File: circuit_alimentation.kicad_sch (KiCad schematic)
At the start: 32 parts, among them U1 STM32-(STM32H745ZIT6)

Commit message: Plein de modifs
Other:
- note added: "À vérifier si peux convertir 5V en 3.3V (voir VDD50USB)"
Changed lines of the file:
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@@
+    (stroke (width 0) (type default))
+  )
+  (wire (pts (xy 25.4 88.9) (xy 31.75 88.9))
     (stroke (width 0) (type default))
   )
@@
     (fill (type none))
   )
+  (arc (start 12.7 99.06) (mid 12.7638 93.8259) (end 16.51 90.17)
+    (stroke (width 0) (type default))
+    (fill (type none))
+  )
   (text "Découplage" (at 215.9 16.51 0)
+    (effects (font (size 1.27 1.27)) (justify left bottom))
+  )
+  (text "À vérifier si peux convertir\n5V en 3.3V (voir VDD50USB)"
+    (at 13.97 102.87 0)
     (effects (font (size 1.27 1.27)) (justify left bottom))
   )
@@
     )
   )
+  (symbol (lib_id "power:GND") (at 25.4 88.9 270) (unit 1)
+    (in_bom yes) (on_board yes) (dnp no) (fields_autoplaced)
+    (property "Reference" "#PWR059" (at 19.05 88.9 0)
+      (effects (font (size 1.27 1.27)) hide)
+    )
+    (property "Value" "GND" (at 21.59 88.9 90)
+      (effects (font (size 1.27 1.27)) (justify right))
+    )
+    (property "Footprint" "" (at 25.4 88.9 0)
+      (effects (font (size 1.27 1.27)) hide)
+    )
+    (property "Datasheet" "" (at 25.4 88.9 0)
+      (effects (font (size 1.27 1.27)) hide)
+    )
+    (pin "1")
+    (instances
+      (project "Payload"
+        (path "/5f62c44b-34ee-4720-b187-b4a520863a8a/b20c1a40-233f-480d-ac91-6f1a7bcdc93c"
+          (reference "#PWR059") (unit 1)
+        )
+      )
+    )
+  )
   (symbol (lib_id "power:+3.3V") (at 250.19 109.22 0) (unit 1)
     (in_bom yes) (on_board yes) (dnp no) (fields_autoplaced)
@@
         )
       )
-    )
-  )
-  (symbol (lib_id "power:GND") (at 31.75 88.9 270) (unit 1)
-    (in_bom yes) (on_board yes) (dnp no) (fields_autoplaced)
-    (property "Reference" "#PWR059" (at 25.4 88.9 0)
-      (effects (font (size 1.27 1.27)) hide)
-    )
-    (property "Value" "GND" (at 27.94 88.9 90)
-      (effects (font (size 1.27 1.27)) (justify right))
-    )
-    (property "Footprint" "" (at 31.75 88.9 0)
-      (effects (font (size 1.27 1.27)) hide)
-    )
-    (property "Datasheet" "" (at 31.75 88.9 0)
-      (effects (font (size 1.27 1.27)) hide)
-    )
-    (pin "1")
-    (instances
-      (project "Payload"
-        (path "/5f62c44b-34ee-4720-b187-b4a520863a8a/b20c1a40-233f-480d-ac91-6f1a7bcdc93c"
-          (reference "#PWR059") (unit 1)
-        )
-      )

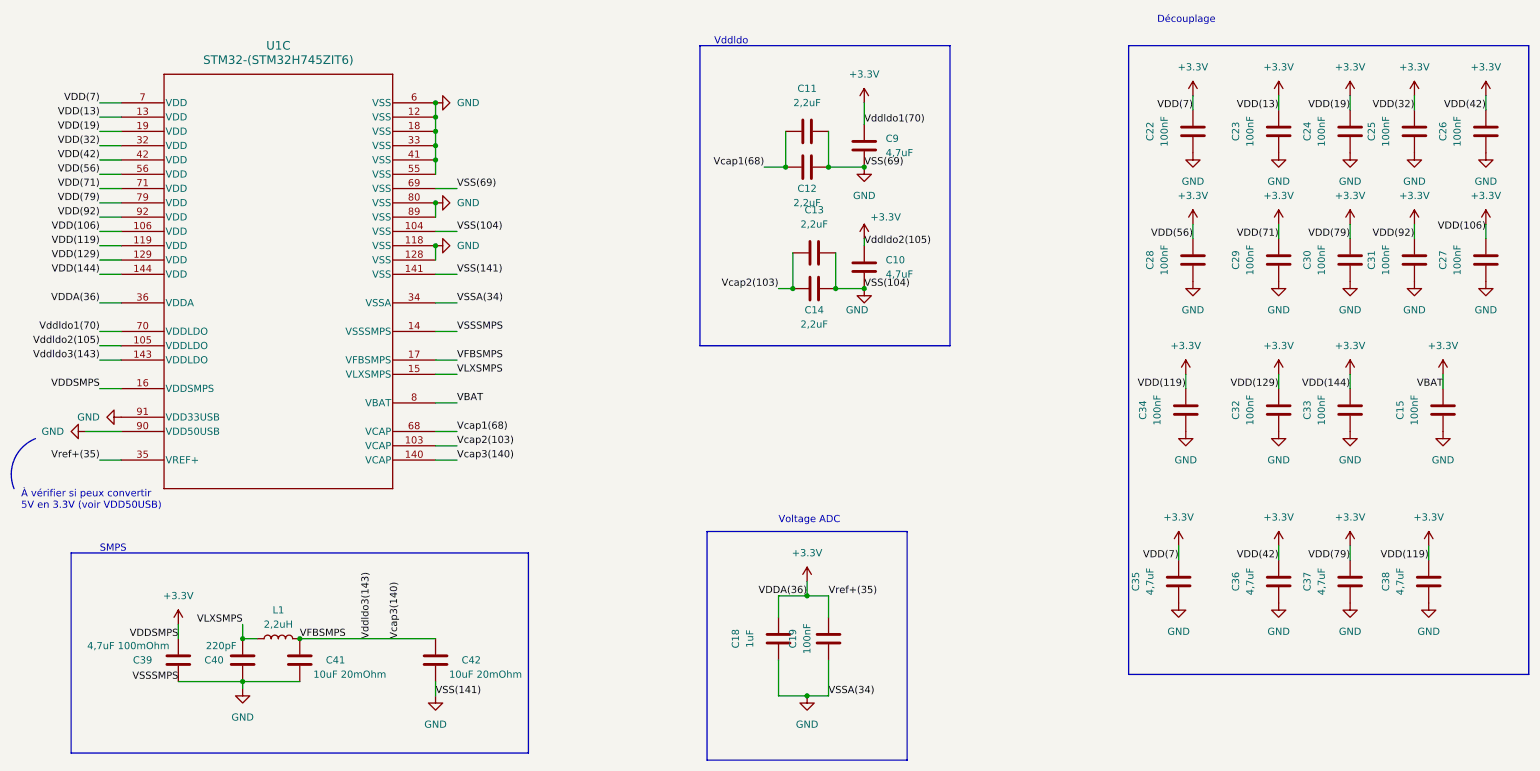
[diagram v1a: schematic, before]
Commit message: Petites modif et assignation des empreintes à 50%
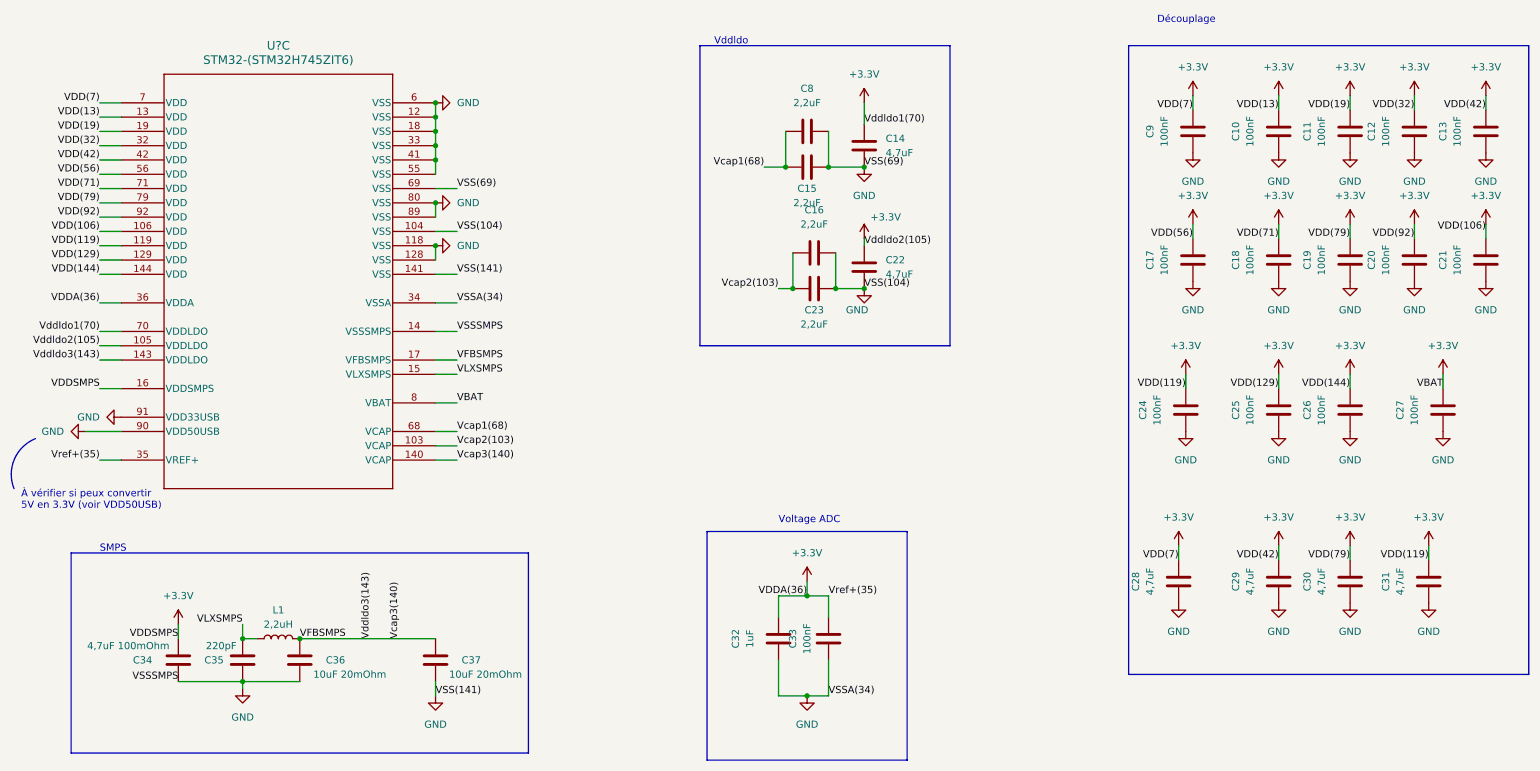
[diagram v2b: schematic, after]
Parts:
- C10: renamed from C23; footprint (none) -> GAUL-Empreintes:cap-0.1uF-(CAPC0603X33N)
- C11: renamed from C24; footprint (none) -> GAUL-Empreintes:cap-0.1uF-(CAPC0603X33N)
- C12: renamed from C25; footprint (none) -> GAUL-Empreintes:cap-0.1uF-(CAPC0603X33N)
- C13: renamed from C26; footprint (none) -> GAUL-Empreintes:cap-0.1uF-(CAPC0603X33N)
- C15: renamed from C12; footprint (none) -> GAUL-Empreintes:cap-2.2uF-(CAPC1005X55N)
- C16: renamed from C13; footprint (none) -> GAUL-Empreintes:cap-2.2uF-(CAPC1005X55N)
- C17: renamed from C28; footprint (none) -> GAUL-Empreintes:cap-0.1uF-(CAPC0603X33N)
- C18: renamed from C29; footprint (none) -> GAUL-Empreintes:cap-0.1uF-(CAPC0603X33N)
- C19: renamed from C30; footprint (none) -> GAUL-Empreintes:cap-0.1uF-(CAPC0603X33N)
- C20: renamed from C31; footprint (none) -> GAUL-Empreintes:cap-0.1uF-(CAPC0603X33N)
- C21: renamed from C27; footprint (none) -> GAUL-Empreintes:cap-0.1uF-(CAPC0603X33N)
- C23: renamed from C14; footprint (none) -> GAUL-Empreintes:cap-2.2uF-(CAPC1005X55N)
- C24: renamed from C34; footprint (none) -> GAUL-Empreintes:cap-0.1uF-(CAPC0603X33N)
- C25: renamed from C32; footprint (none) -> GAUL-Empreintes:cap-0.1uF-(CAPC0603X33N)
- C26: renamed from C33; footprint (none) -> GAUL-Empreintes:cap-0.1uF-(CAPC0603X33N)
- C27: renamed from C15; footprint (none) -> GAUL-Empreintes:cap-0.1uF-(CAPC0603X33N)
- C28: renamed from C35; footprint (none) -> GAUL-Empreintes:cap-4.7uF-(CAPC1608X90N)
- C29: renamed from C36; footprint (none) -> GAUL-Empreintes:cap-4.7uF-(CAPC1608X90N)
- C30: renamed from C37; footprint (none) -> GAUL-Empreintes:cap-4.7uF-(CAPC1608X90N)
- C31: renamed from C38; footprint (none) -> GAUL-Empreintes:cap-4.7uF-(CAPC1608X90N)
- C32: renamed from C18; footprint (none) -> GAUL-Empreintes:cap-1uF-(CAPC0603X35N)
- C33: renamed from C19; footprint (none) -> GAUL-Empreintes:cap-0.1uF-(CAPC0603X33N)
- C9: renamed from C22; footprint (none) -> GAUL-Empreintes:cap-0.1uF-(CAPC0603X33N)
- U?: renamed from U1; footprint LQFP-144 -> GAUL-Empreintes:STM32
- renumbered C9 to C14, C10 to C22, C39 to C34, C40 to C35, C41 to C36, C42 to C37, C11 to C8

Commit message: Début PCB
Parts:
- C10, C11, C12, C13, C17, C18, C19, C20, C21, C24, C25, C26, C27, C33, C9: footprint GAUL-Empreintes:cap-0.1uF-(CAPC0603X33N) -> Capacitor_SMD:C_0603_1608Metric_Pad1.08x0.95mm_HandSolder
- C14, C22, C35, C8: footprint (none) -> Capacitor_SMD:C_0603_1608Metric_Pad1.08x0.95mm_HandSolder
- C15, C16, C23: footprint GAUL-Empreintes:cap-2.2uF-(CAPC1005X55N) -> Capacitor_SMD:C_0603_1608Metric_Pad1.08x0.95mm_HandSolder
- C28, C29, C30, C31: footprint GAUL-Empreintes:cap-4.7uF-(CAPC1608X90N) -> Capacitor_SMD:C_0603_1608Metric_Pad1.08x0.95mm_HandSolder
- C32: footprint GAUL-Empreintes:cap-1uF-(CAPC0603X35N) -> Capacitor_SMD:C_0603_1608Metric_Pad1.08x0.95mm_HandSolder
- C34: footprint (none) -> GAUL-Empreintes:cap-4.7uF-75R-(CAPMP7.6X4.3_3.1N_KEM-L)
- C36, C37: footprint (none) -> GAUL-Empreintes:cap-10uF-50R-(CAPMP7.6X4.3_4.3N_KEM-L)
- L1: footprint (none) -> Inductor_SMD:L_0603_1608Metric_Pad1.05x0.95mm_HandSolder
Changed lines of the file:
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@@
       (effects (font (size 1.27 1.27)))
     )
-    (property "Footprint" "GAUL-Empreintes:cap-0.1uF-(CAPC0603X33N)" (at 273.3548 54.61 0)
+    (property "Footprint" "Capacitor_SMD:C_0603_1608Metric_Pad1.08x0.95mm_HandSolder" (at 273.3548 54.61 0)
       (effects (font (size 1.27 1.27)) hide)
     )
@@
       (effects (font (size 1.27 1.27)))
     )
-    (property "Footprint" "GAUL-Empreintes:cap-0.1uF-(CAPC0603X33N)" (at 260.6548 54.61 0)
+    (property "Footprint" "Capacitor_SMD:C_0603_1608Metric_Pad1.08x0.95mm_HandSolder" (at 260.6548 54.61 0)
       (effects (font (size 1.27 1.27)) hide)
     )
@@
       (effects (font (size 1.27 1.27)))
     )
-    (property "Footprint" "GAUL-Empreintes:cap-0.1uF-(CAPC0603X33N)" (at 236.5248 54.61 0)
+    (property "Footprint" "Capacitor_SMD:C_0603_1608Metric_Pad1.08x0.95mm_HandSolder" (at 236.5248 54.61 0)
       (effects (font (size 1.27 1.27)) hide)
     )
@@
       (effects (font (size 1.27 1.27)))
     )
-    (property "Footprint" "GAUL-Empreintes:cap-2.2uF-(CAPC1005X55N)" (at 158.75 62.5348 0)
+    (property "Footprint" "Capacitor_SMD:C_0603_1608Metric_Pad1.08x0.95mm_HandSolder" (at 158.75 62.5348 0)
       (effects (font (size 1.27 1.27)) hide)
     )
@@
       (effects (font (size 1.27 1.27)))
     )
-    (property "Footprint" "GAUL-Empreintes:cap-4.7uF-(CAPC1608X90N)" (at 218.7448 111.76 0)
+    (property "Footprint" "Capacitor_SMD:C_0603_1608Metric_Pad1.08x0.95mm_HandSolder" (at 218.7448 111.76 0)
       (effects (font (size 1.27 1.27)) hide)
     )
@@
       (effects (font (size 1.27 1.27)))
     )
-    (property "Footprint" "GAUL-Empreintes:cap-2.2uF-(CAPC1005X55N)" (at 158.75 56.1848 0)
+    (property "Footprint" "Capacitor_SMD:C_0603_1608Metric_Pad1.08x0.95mm_HandSolder" (at 158.75 56.1848 0)
       (effects (font (size 1.27 1.27)) hide)
     )
@@
       (effects (font (size 1.27 1.27)))
     )
-    (property "Footprint" "GAUL-Empreintes:cap-1uF-(CAPC0603X35N)" (at 147.6248 121.92 0)
+    (property "Footprint" "Capacitor_SMD:C_0603_1608Metric_Pad1.08x0.95mm_HandSolder" (at 147.6248 121.92 0)
       (effects (font (size 1.27 1.27)) hide)
     )
@@
       (effects (font (size 1.27 1.27)))
     )
-    (property "Footprint" "GAUL-Empreintes:cap-0.1uF-(CAPC0603X33N)" (at 221.2848 31.75 0)
+    (property "Footprint" "Capacitor_SMD:C_0603_1608Metric_Pad1.08x0.95mm_HandSolder" (at 221.2848 31.75 0)
       (effects (font (size 1.27 1.27)) hide)
     )
@@
       (effects (font (size 1.27 1.27)) (justify right))
     )
-    (property "Footprint" "" (at 162.8648 55.88 0)
+    (property "Footprint" "Capacitor_SMD:C_0603_1608Metric_Pad1.08x0.95mm_HandSolder" (at 162.8648 55.88 0)
       (effects (font (size 1.27 1.27)) hide)
     )
@@
       (effects (font (size 1.27 1.27)))
     )
-    (property "Footprint" "GAUL-Empreintes:cap-4.7uF-(CAPC1608X90N)" (at 263.1948 111.76 0)
+    (property "Footprint" "Capacitor_SMD:C_0603_1608Metric_Pad1.08x0.95mm_HandSolder" (at 263.1948 111.76 0)
       (effects (font (size 1.27 1.27)) hide)
     )
@@
       (effects (font (size 1.27 1.27)))
     )
-    (property "Footprint" "" (at 86.6648 125.73 0)
+    (property "Footprint" "GAUL-Empreintes:cap-10uF-50R-(CAPMP7.6X4.3_4.3N_KEM-L)" (at 86.6648 125.73 0)
       (effects (font (size 1.27 1.27)) hide)
     )
@@
       (effects (font (size 1.27 1.27)))
     )
-    (property "Footprint" "GAUL-Empreintes:cap-4.7uF-(CAPC1608X90N)" (at 249.2248 111.76 0)
+    (property "Footprint" "Capacitor_SMD:C_0603_1608Metric_Pad1.08x0.95mm_HandSolder" (at 249.2248 111.76 0)
       (effects (font (size 1.27 1.27)) hide)
     )
@@
       (effects (font (size 1.27 1.27)))
     )
-    (property "Footprint" "" (at 59.69 125.73 0)
+    (property "Footprint" "Inductor_SMD:L_0603_1608Metric_Pad1.05x0.95mm_HandSolder" (at 59.69 125.73 0)
       (effects (font (size 1.27 1.27)) hide)
     )
@@
       (effects (font (size 1.27 1.27)))
     )
-    (property "Footprint" "GAUL-Empreintes:cap-0.1uF-(CAPC0603X33N)" (at 236.5248 81.28 0)
+    (property "Footprint" "Capacitor_SMD:C_0603_1608Metric_Pad1.08x0.95mm_HandSolder" (at 236.5248 81.28 0)
       (effects (font (size 1.27 1.27)) hide)
     )
@@
       (effects (font (size 1.27 1.27)))
     )
-    (property "Footprint" "GAUL-Empreintes:cap-0.1uF-(CAPC0603X33N)" (at 249.2248 31.75 0)
+    (property "Footprint" "Capacitor_SMD:C_0603_1608Metric_Pad1.08x0.95mm_HandSolder" (at 249.2248 31.75 0)
       (effects (font (size 1.27 1.27)) hide)
     )
@@
       (effects (font (size 1.27 1.27)))
     )
-    (property "Footprint" "GAUL-Empreintes:cap-0.1uF-(CAPC0603X33N)" (at 260.6548 31.75 0)
+    (property "Footprint" "Capacitor_SMD:C_0603_1608Metric_Pad1.08x0.95mm_HandSolder" (at 260.6548 31.75 0)
       (effects (font (size 1.27 1.27)) hide)
     )
@@
       (effects (font (size 1.27 1.27)))
     )
-    (property "Footprint" "GAUL-Empreintes:cap-0.1uF-(CAPC0603X33N)" (at 221.2848 54.61 0)
+    (property "Footprint" "Capacitor_SMD:C_0603_1608Metric_Pad1.08x0.95mm_HandSolder" (at 221.2848 54.61 0)
       (effects (font (size 1.27 1.27)) hide)
     )
@@
       (effects (font (size 1.27 1.27)))
     )
-    (property "Footprint" "GAUL-Empreintes:cap-0.1uF-(CAPC0603X33N)" (at 249.2248 81.28 0)
+    (property "Footprint" "Capacitor_SMD:C_0603_1608Metric_Pad1.08x0.95mm_HandSolder" (at 249.2248 81.28 0)
       (effects (font (size 1.27 1.27)) hide)
     )
@@
       (effects (font (size 1.27 1.27)))
     )
-    (property "Footprint" "" (at 42.8752 133.35 0)
+    (property "Footprint" "GAUL-Empreintes:cap-4.7uF-75R-(CAPMP7.6X4.3_3.1N_KEM-L)" (at 42.8752 133.35 0)
       (effects (font (size 1.27 1.27)) hide)
     )
@@
       (effects (font (size 1.27 1.27)))
     )
-    (property "Footprint" "GAUL-Empreintes:cap-4.7uF-(CAPC1608X90N)" (at 236.5248 111.76 0)
+    (property "Footprint" "Capacitor_SMD:C_0603_1608Metric_Pad1.08x0.95mm_HandSolder" (at 236.5248 111.76 0)
       (effects (font (size 1.27 1.27)) hide)
     )
@@
       (effects (font (size 1.27 1.27)))
     )
-    (property "Footprint" "GAUL-Empreintes:cap-0.1uF-(CAPC0603X33N)" (at 236.5248 31.75 0)
+    (property "Footprint" "Capacitor_SMD:C_0603_1608Metric_Pad1.08x0.95mm_HandSolder" (at 236.5248 31.75 0)
       (effects (font (size 1.27 1.27)) hide)
     )
@@
       (effects (font (size 1.27 1.27)))
     )
-    (property "Footprint" "GAUL-Empreintes:cap-2.2uF-(CAPC1005X55N)" (at 157.48 40.9448 0)
+    (property "Footprint" "Capacitor_SMD:C_0603_1608Metric_Pad1.08x0.95mm_HandSolder" (at 157.48 40.9448 0)
       (effects (font (size 1.27 1.27)) hide)
     )
@@
       (effects (font (size 1.27 1.27)))
     )
-    (property "Footprint" "" (at 54.3052 133.35 0)
+    (property "Footprint" "Capacitor_SMD:C_0603_1608Metric_Pad1.08x0.95mm_HandSolder" (at 54.3052 133.35 0)
       (effects (font (size 1.27 1.27)) hide)
     )
@@
       (effects (font (size 1.27 1.27)))
     )
-    (property "Footprint" "" (at 157.48 34.5948 0)
+    (property "Footprint" "Capacitor_SMD:C_0603_1608Metric_Pad1.08x0.95mm_HandSolder" (at 157.48 34.5948 0)
       (effects (font (size 1.27 1.27)) hide)
     )
@@
       (effects (font (size 1.27 1.27)))
     )
-    (property "Footprint" "GAUL-Empreintes:cap-0.1uF-(CAPC0603X33N)" (at 249.2248 54.61 0)
+    (property "Footprint" "Capacitor_SMD:C_0603_1608Metric_Pad1.08x0.95mm_HandSolder" (at 249.2248 54.61 0)
       (effects (font (size 1.27 1.27)) hide)
     )
@@
       (effects (font (size 1.27 1.27)))
     )
-    (property "Footprint" "GAUL-Empreintes:cap-0.1uF-(CAPC0603X33N)" (at 156.5148 121.92 0)
+    (property "Footprint" "Capacitor_SMD:C_0603_1608Metric_Pad1.08x0.95mm_HandSolder" (at 156.5148 121.92 0)
       (effects (font (size 1.27 1.27)) hide)
     )
@@
       (effects (font (size 1.27 1.27)))
     )
-    (property "Footprint" "GAUL-Empreintes:cap-0.1uF-(CAPC0603X33N)" (at 265.7348 81.28 0)
+    (property "Footprint" "Capacitor_SMD:C_0603_1608Metric_Pad1.08x0.95mm_HandSolder" (at 265.7348 81.28 0)
       (effects (font (size 1.27 1.27)) hide)
     )
@@
       (effects (font (size 1.27 1.27)))
     )
-    (property "Footprint" "" (at 62.5348 125.73 0)
+    (property "Footprint" "GAUL-Empreintes:cap-10uF-50R-(CAPMP7.6X4.3_4.3N_KEM-L)" (at 62.5348 125.73 0)
       (effects (font (size 1.27 1.27)) hide)
     )
@@
       (effects (font (size 1.27 1.27)))
     )
-    (property "Footprint" "GAUL-Empreintes:cap-0.1uF-(CAPC0603X33N)" (at 273.3548 31.75 0)
+    (property "Footprint" "Capacitor_SMD:C_0603_1608Metric_Pad1.08x0.95mm_HandSolder" (at 273.3548 31.75 0)
       (effects (font (size 1.27 1.27)) hide)
     )
@@
       (effects (font (size 1.27 1.27)) (justify right))
     )
-    (property "Footprint" "" (at 162.8648 34.29 0)
+    (property "Footprint" "Capacitor_SMD:C_0603_1608Metric_Pad1.08x0.95mm_HandSolder" (at 162.8648 34.29 0)
       (effects (font (size 1.27 1.27)) hide)
     )
@@
       (effects (font (size 1.27 1.27)))
     )
-    (property "Footprint" "GAUL-Empreintes:cap-0.1uF-(CAPC0603X33N)" (at 220.0148 81.28 0)
-      (effects (font (size 1.27 1.27)) hide)
-    )
+    (property "Footprint" "Capacitor_SMD:C_0603_1608Metric_Pad1.08x0.95mm_HandSolder" (at 220.0148 81.28 0)
+      (effects (font (size 1.27 1.27)) hide)
+    )
